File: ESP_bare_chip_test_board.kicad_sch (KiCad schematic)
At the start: 0 parts

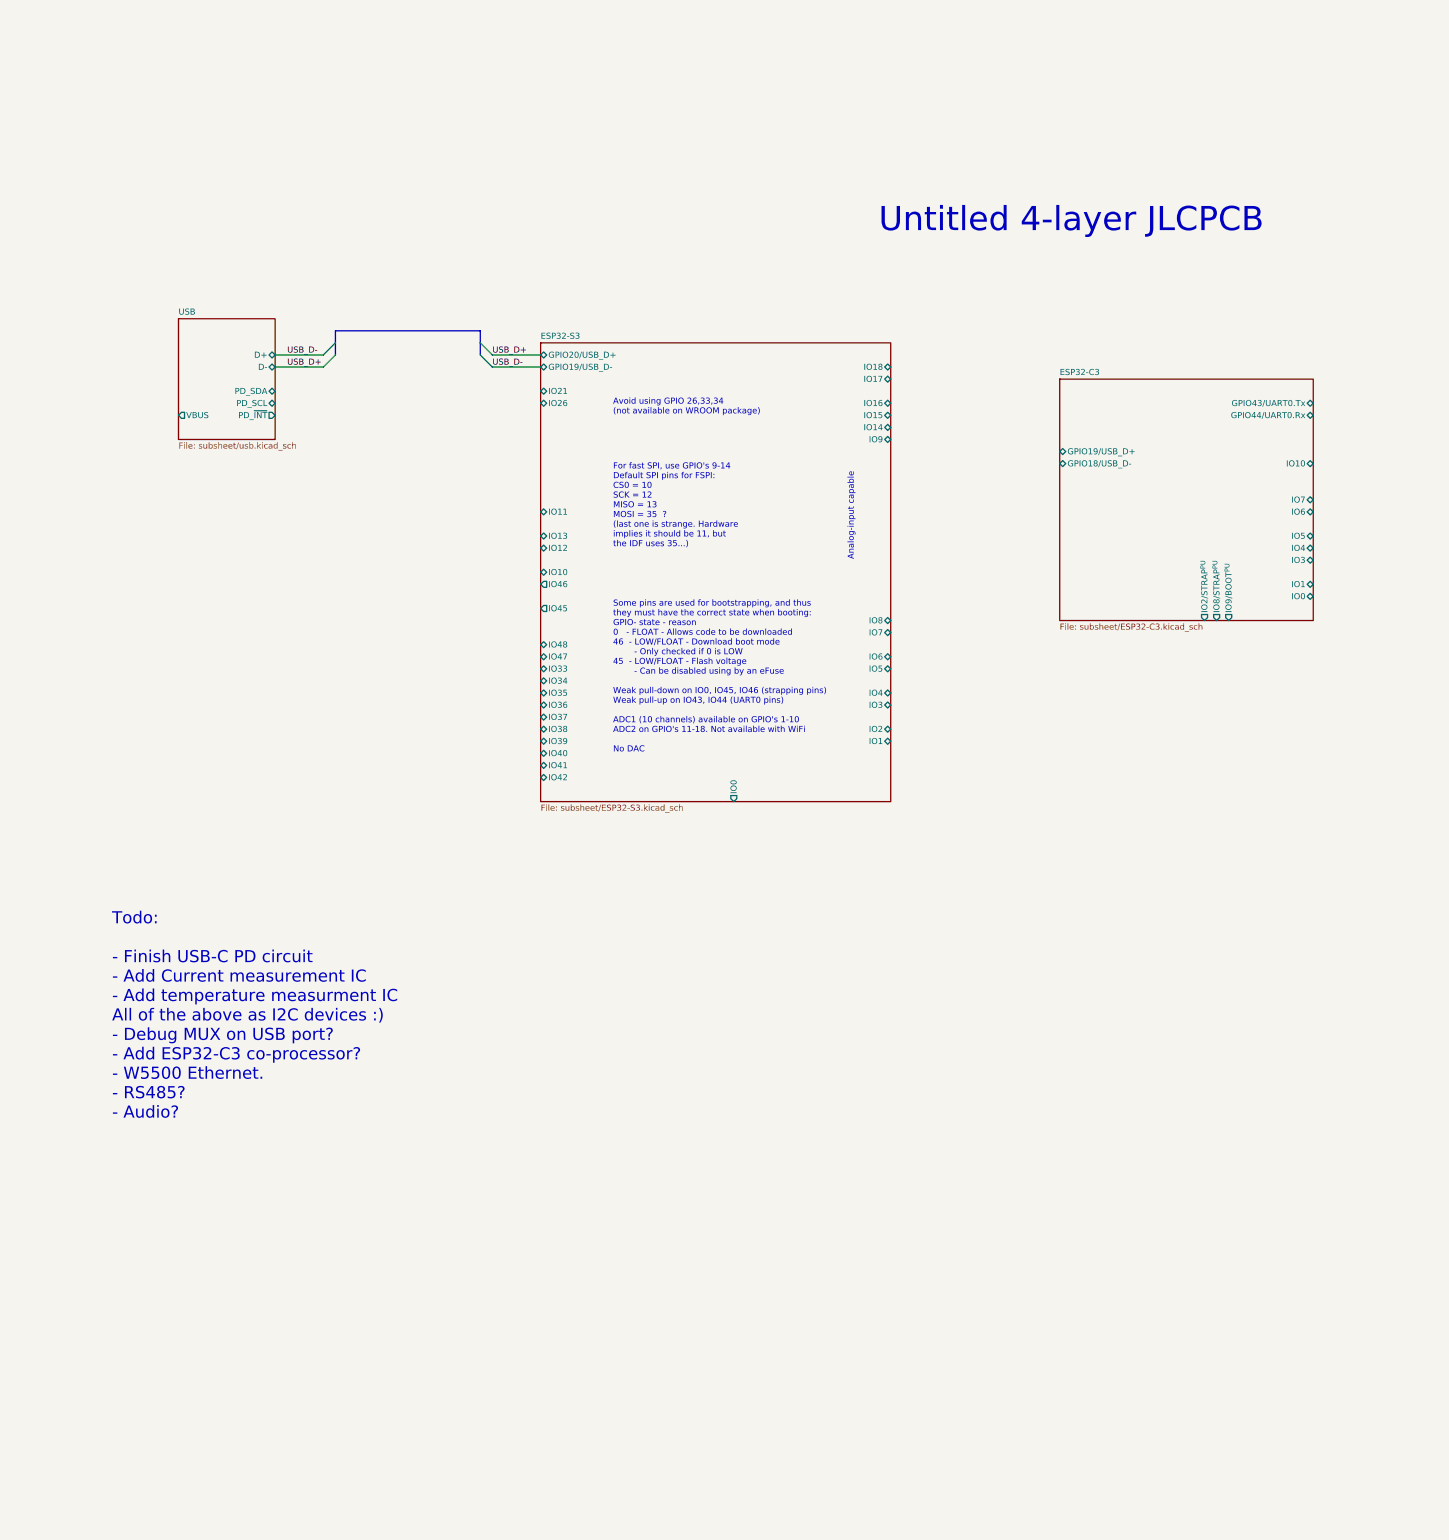
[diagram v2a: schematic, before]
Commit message: Add 5v and 3v3 buck regulators, brige rectifier
Buck regulators are copied from existing designs. 5V regulator needs to
be reworked though; due to ESD vulnerability.

Added 4 diodes in bridge rectifier configuration. Provides a simpler
solution than the polarity-protected eFuse. Due to how the
buck-regulators work, it should be fine for any voltage from ~4.8V 17V
(max Vin of buck regulator). Downside is icnreased power-dissipation,
but since this board is not intended to use a lot of current it should
be good (the USB port can bypass this too, but only for 5V)
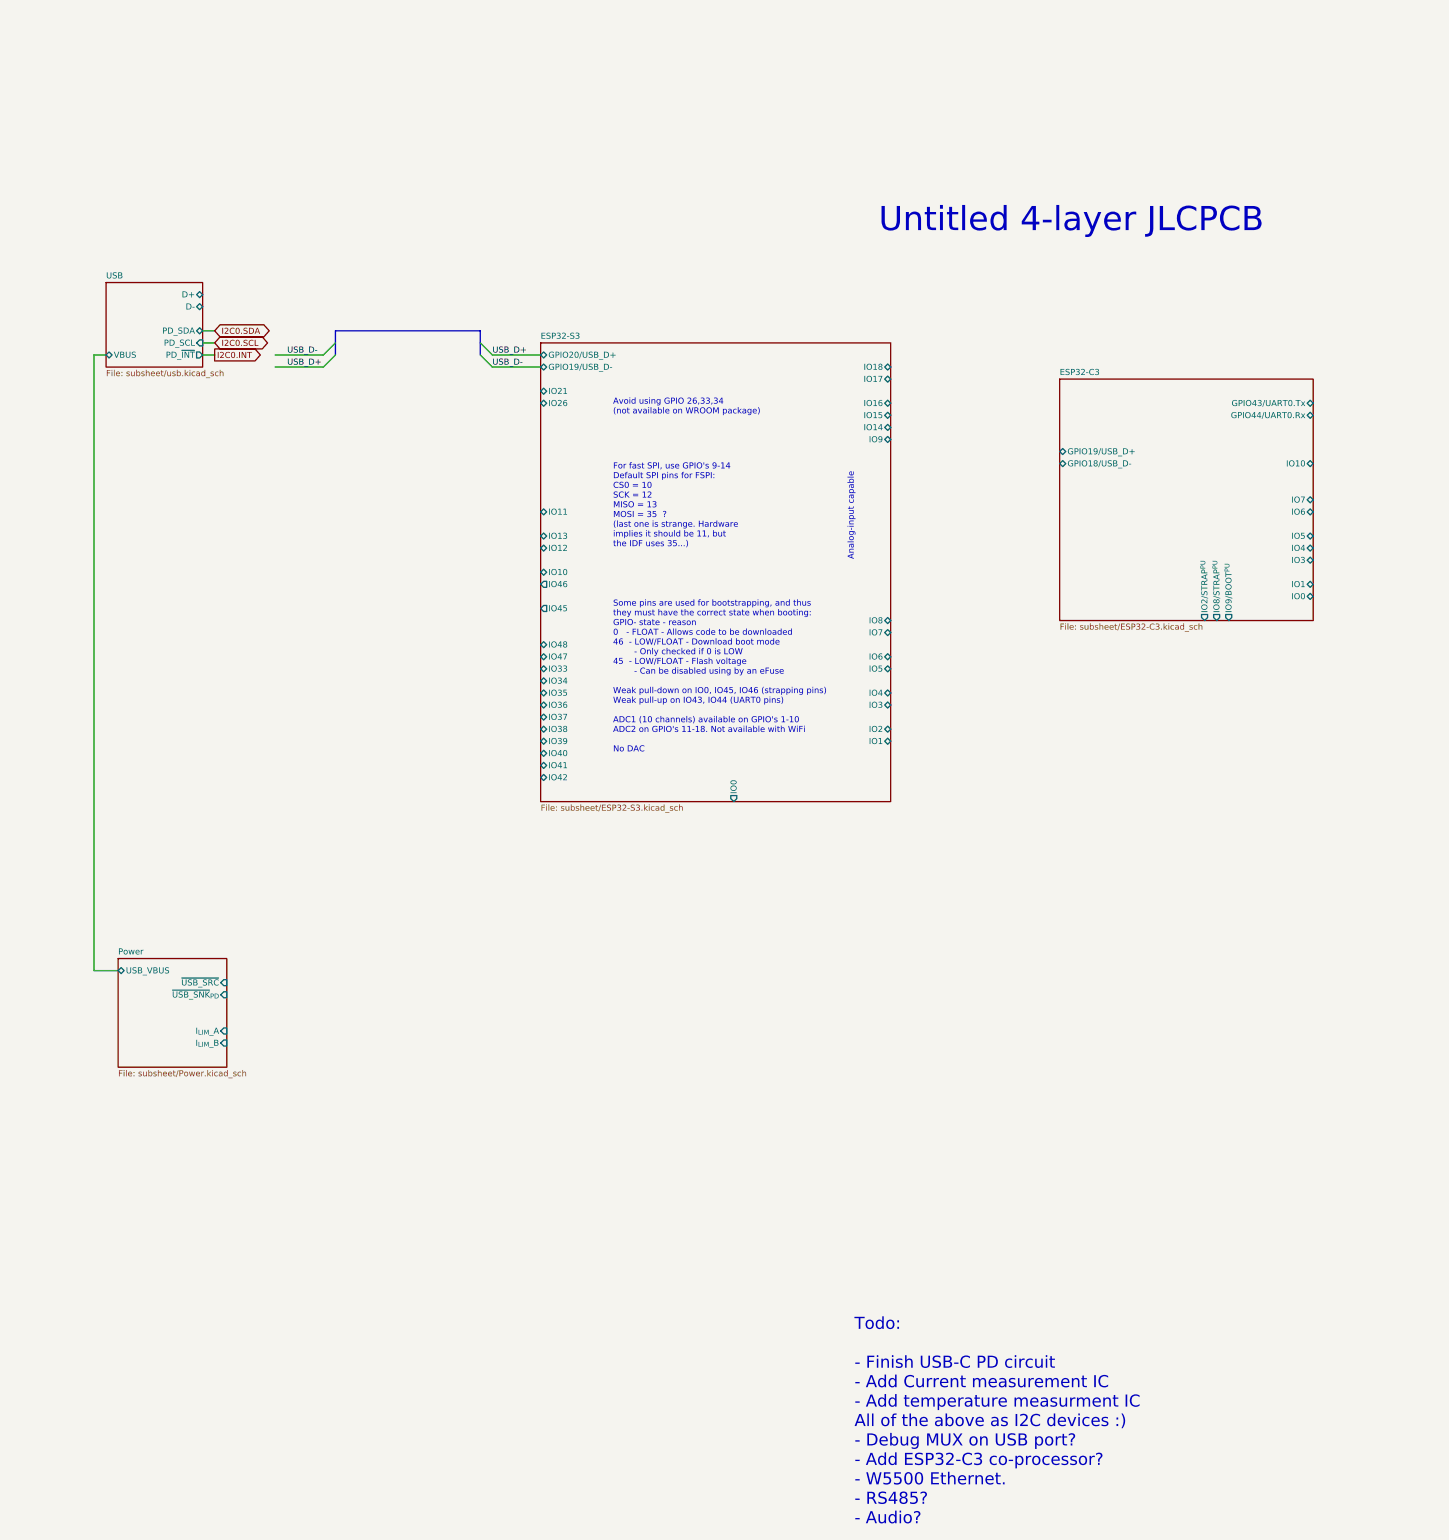
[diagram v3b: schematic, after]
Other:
- added sheet Power (subsheet/Power.kicad_sch)
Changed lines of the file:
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@@
+		)
+	)
+	(wire
+		(pts
+			(xy 15.24 33.02) (xy 15.24 162.56)
+		)
+		(stroke
+			(width 0)
+			(type default)
 		)
 	)
@@
 		)
 	)
+	(wire
+		(pts
+			(xy 17.78 33.02) (xy 15.24 33.02)
+		)
+		(stroke
+			(width 0)
+			(type default)
+		)
+	)
+	(wire
+		(pts
+			(xy 15.24 162.56) (xy 20.32 162.56)
+		)
+		(stroke
+			(width 0)
+			(type default)
+		)
+	)
 	(bus
 		(pts
@@
 	(wire
 		(pts
+			(xy 38.1 27.94) (xy 40.64 27.94)
+		)
+		(stroke
+			(width 0)
+			(type default)
+		)
+	)
+	(wire
+		(pts
 			(xy 99.06 33.02) (xy 109.22 33.02)
+		)
+		(stroke
+			(width 0)
+			(type default)
+		)
+	)
+	(wire
+		(pts
+			(xy 38.1 33.02) (xy 40.64 33.02)
+		)
+		(stroke
+			(width 0)
+			(type default)
+		)
+	)
+	(wire
+		(pts
+			(xy 38.1 30.48) (xy 40.64 30.48)
 		)
 		(stroke
@@
 	(text "Todo:\n\n- Finish USB-C PD circuit\n- Add Current measurement IC\n- Add temperature measurment IC\nAll of the above as I2C devices :)\n- Debug MUX on USB port?\n- Add ESP32-C3 co-processor?\n- W5500 Ethernet.\n- RS485?\n- Audio?"
 		(exclude_from_sim no)
-		(at 19.05 194.056 0)
+		(at 175.26 279.4 0)
 		(effects
 			(font
@@
 			)
 			(justify left bottom)
+		)
+	)
+	(global_label "I2C0.INT"
+		(shape output)
+		(at 40.64 33.02 0)
+		(fields_autoplaced yes)
+		(effects
+			(font
+				(size 1.27 1.27)
+			)
+			(justify left)
+		)
+		(property "Intersheetrefs" "${INTERSHEET_REFS}"
+			(at 51.4267 33.02 0)
+			(effects
+				(font
+					(size 1.27 1.27)
+				)
+				(justify left)
+				(hide yes)
+			)
+		)
+	)
+	(global_label "I2C0.SDA"
+		(shape bidirectional)
+		(at 40.64 27.94 0)
+		(fields_autoplaced yes)
+		(effects
+			(font
+				(size 1.27 1.27)
+			)
+			(justify left)
+		)
+		(property "Intersheetrefs" "${INTERSHEET_REFS}"
+			(at 53.2032 27.94 0)
+			(effects
+				(font
+					(size 1.27 1.27)
+				)
+				(justify left)
+				(hide yes)
+			)
+		)
+	)
+	(global_label "I2C0.SCL"
+		(shape bidirectional)
+		(at 40.64 30.48 0)
+		(fields_autoplaced yes)
+		(effects
+			(font
+				(size 1.27 1.27)
+			)
+			(justify left)
+		)
+		(property "Intersheetrefs" "${INTERSHEET_REFS}"
+			(at 53.1427 30.48 0)
+			(effects
+				(font
+					(size 1.27 1.27)
+				)
+				(justify left)
+				(hide yes)
+			)
 		)
 	)
@@
 	)
 	(sheet
-		(at 33.02 25.4)
-		(size 20.32 25.4)
+		(at 20.32 160.02)
+		(size 22.86 22.86)
 		(fields_autoplaced yes)
 		(stroke
@@
 			(color 255 229 191 1.0000)
 		)
-		(property "Sheetname" "USB"
-			(at 33.02 24.6884 0)
+		(property "Sheetname" "Power"
+			(at 20.32 159.3084 0)
 			(effects
 				(font
@@
 			)
 		)
-		(property "Sheetfile" "subsheet/usb.kicad_sch"
-			(at 33.02 51.3846 0)
+		(property "Sheetfile" "subsheet/Power.kicad_sch"
+			(at 20.32 183.4646 0)
 			(effects
 				(font
@@
 			)
 		)
-		(pin "D+" bidirectional
-			(at 53.34 33.02 0)
-			(effects
-				(font
-					(size 1.27 1.27)
-				)
-				(justify right)
-			)
-		)
-		(pin "D-" bidirectional
-			(at 53.34 35.56 0)
-			(effects
-				(font
-					(size 1.27 1.27)
-				)
-				(justify right)
-			)
-		)
-		(pin "PD_~{INT}" output
-			(at 53.34 45.72 0)
-			(effects
-				(font
-					(size 1.27 1.27)
-				)
-				(justify right)
-			)
-		)
-		(pin "PD_SCL" bidirectional
-			(at 53.34 43.18 0)
-			(effects
-				(font
-					(size 1.27 1.27)
-				)
-				(justify right)
-			)
-		)
-		(pin "PD_SDA" bidirectional
-			(at 53.34 40.64 0)
-			(effects
-				(font
-					(size 1.27 1.27)
-				)
-				(justify right)
-			)
-		)
-		(pin "VBUS" output
-			(at 33.02 45.72 180)
-			(effects
-				(font
-					(size 1.27 1.27)
-				)
-				(justify left)
+		(pin "USB_VBUS" bidirectional
+			(at 20.32 162.56 180)
+			(effects
+				(font
+					(size 1.27 1.27)
+				)
+				(justify left)
+			)
+		)
+		(pin "~{USB_SRC}" input
+			(at 43.18 165.1 0)
+			(effects
+				(font
+					(size 1.27 1.27)
+				)
+				(justify right)
+			)
+		)
+		(pin "~{USB_SNK}_{PD}" input
+			(at 43.18 167.64 0)
+			(effects
+				(font
+					(size 1.27 1.27)
+				)
+				(justify right)
+			)
+		)
+		(pin "I_{LIM}_B" input
+			(at 43.18 177.8 0)
+			(effects
+				(font
+					(size 1.27 1.27)
+				)
+				(justify right)
+			)
+		)
+		(pin "I_{LIM}_A" input
+			(at 43.18 175.26 0)
+			(effects
+				(font
+					(size 1.27 1.27)
+				)
+				(justify right)
 			)
 		)
@@
 				)
 			)
+		)
+	)
+	(sheet
+		(at 17.78 17.78)
+		(size 20.32 17.78)
+		(fields_autoplaced yes)
+		(stroke
+			(width 0.1524)
+			(type solid)
+		)
+		(fill
+			(color 255 229 191 1.0000)
+		)
+		(property "Sheetname" "USB"
+			(at 17.78 17.0684 0)
+			(effects
+				(font
+					(size 1.27 1.27)
+				)
+				(justify left bottom)
+			)
+		)
+		(property "Sheetfile" "subsheet/usb.kicad_sch"
+			(at 17.78 36.1446 0)
+			(effects
+				(font
+					(size 1.27 1.27)
+				)
+				(justify left top)
+			)
+		)
+		(pin "D+" bidirectional
+			(at 38.1 20.32 0)
+			(effects
+				(font
+					(size 1.27 1.27)
+				)
+				(justify right)
+			)
+		)
+		(pin "D-" bidirectional
+			(at 38.1 22.86 0)
+			(effects
+				(font
+					(size 1.27 1.27)
+				)
+				(justify right)
+			)
+		)
+		(pin "PD_~{INT}" output
+			(at 38.1 33.02 0)
+			(effects
+				(font
+					(size 1.27 1.27)
+				)
+				(justify right)
+			)
+		)
+		(pin "PD_SDA" bidirectional
+			(at 38.1 27.94 0)
+			(effects
+				(font
+					(size 1.27 1.27)
+				)
+				(justify right)
+			)
+		)
+		(pin "VBUS" bidirectional
+			(at 17.78 33.02 180)
+			(effects
+				(font
+					(size 1.27 1.27)
+				)
+				(justify left)
+			)
+		)
+		(pin "PD_SCL" input
+			(at 38.1 30.48 0)
+			(effects
+				(font
+					(size 1.27 1.27)
+				)
+				(justify right)
+			)
+		)
+		(instances
+			(project "ESP_bare_chip_test_board"
+				(path "/45b6f84a-e69b-48be-a49b-bc68872e2c15"
+					(page "8")
+				)
+			)

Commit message: PCB changes, added useful connectors
Added a whole bunch of things that should make it useful - e.g.
ethernet, an extra flash chip for general storage, piicodev connectors
for I2C.

Also added a GPIB connector footprint; dev-board version worked nicely,
but may as well make this work for that too. Saves bying dev boards : )
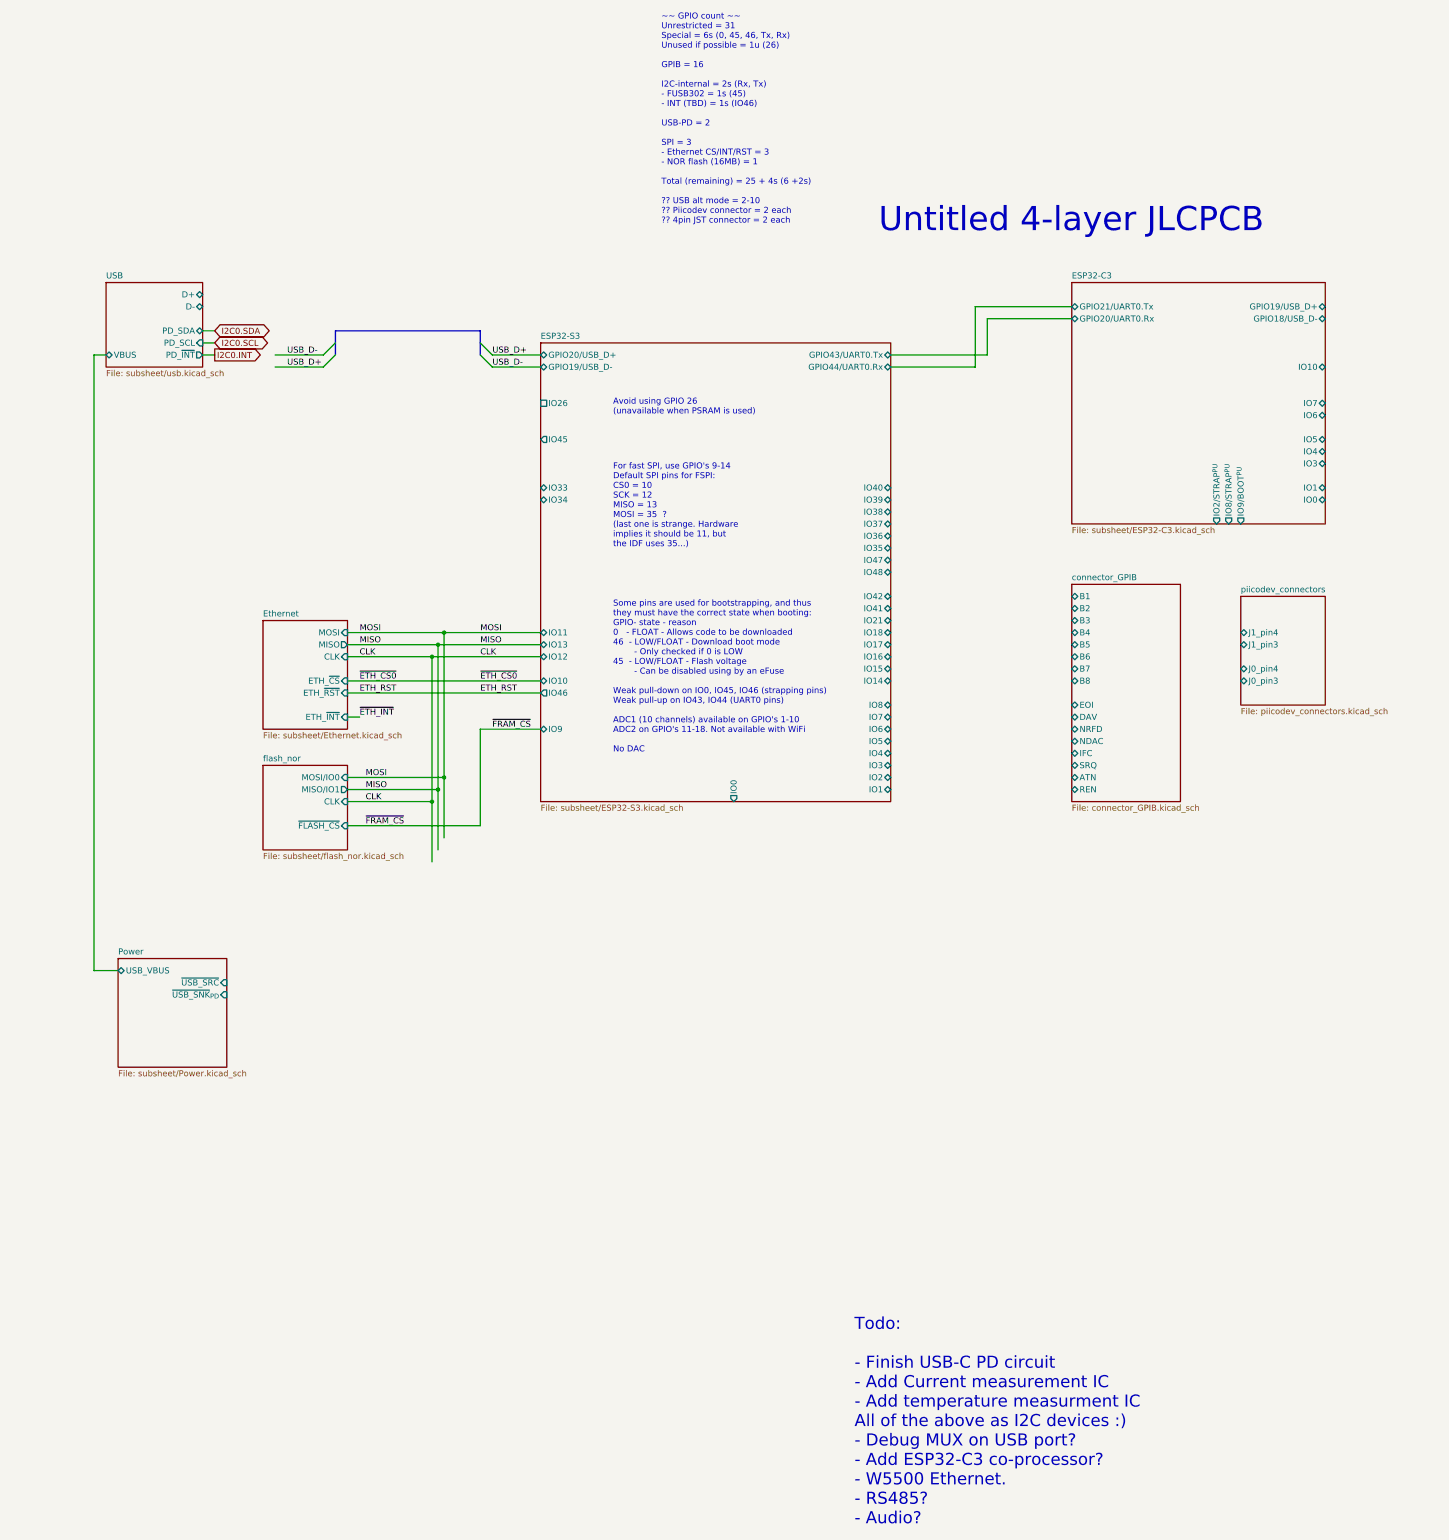
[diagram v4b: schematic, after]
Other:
- added sheet Ethernet (subsheet/Ethernet.kicad_sch)
- added sheet connector_GPIB (connector_GPIB.kicad_sch)
- added sheet flash_nor (subsheet/flash_nor.kicad_sch)
- added sheet piicodev_connectors (piicodev_connectors.kicad_sch)
- sheet ESP32-C3 ports: added GPIO20/UART0.Rx, GPIO21/UART0.Tx; removed GPIO43/UART0.Tx, GPIO44/UART0.Rx
- sheet ESP32-S3 ports: added GPIO43/UART0.Tx, GPIO44/UART0.Rx; removed none
- sheet Power ports: added none; removed I_{LIM}_A, I_{LIM}_B
- note added: "Avoid using GPIO 26 (unavailable when PSRAM is used)"
- note added: "~~ GPIO count ~~ Unrestricted = 31 Special = 6s (0, 45, 46, Tx, Rx) Unused if possible = 1u (26) GPIB = 16 I2C-internal = 2s (Rx, Tx) - FUSB302 = 1s (45) - INT (TBD) = 1s (IO46) USB-PD = 2 SPI = 3 - Ethernet CS/INT/RST = 3 - NOR flash (16MB) = 1 Total (remaining) = 25 + 4s (6 +2s) ?? USB alt mode = 2-10 ?? Piicodev connector = 2 each ?? 4pin JST connector = 2 each"
- note removed: "Analog-input capable"
- note removed: "Avoid using GPIO 26,33,34 (not available on WROOM package)"
